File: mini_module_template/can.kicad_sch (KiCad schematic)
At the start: 8 parts, among them SW4 SW_DIP_x01, U4 SN65HVD232

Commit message: Leyout rev 1
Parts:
- removed C14: 100n, Capacitor_SMD:C_0402_1005Metric, symbol Device:C
- removed U4: SN65HVD232, Package_SO:SOIC-8_3.9x4.9mm_P1.27mm, symbol Interface_CAN_LIN:SN65HVD232
- added C36: 100n, Capacitor_SMD:C_0402_1005Metric, symbol Device:C
- added IC1: TJA1044GTK_3Z, SON65P300X300X100-9N-D, symbol TJA1044GTK_3Z:TJA1044GTK_3Z
- added R38: 10k, Resistor_SMD:R_0402_1005Metric, symbol Device:R
- renumbered D3 to D8, D4 to D9, R9 to R36, R20 to R37, R21 to R39
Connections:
- net +3V3: now also IC1.5 (VIO)
- net CAN_H: now also SW4.2, IC1.7 (CANH); no longer R39.1
- net CAN_L: now also R39.1, IC1.6 (CANL); no longer SW4.2
- net CAN_RXD: now also IC1.4 (RXD)
- net CAN_TXD: now also IC1.1 (TXD)
- net GND: now also C36.2, IC1.2 (GND), R38.1
- new net: IC1.8 (STB), R38.2
- new net +5V: C36.1, IC1.3 (VCC)
- no-connect marks 0 -> 1
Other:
- moved on the sheet: R39, SW4

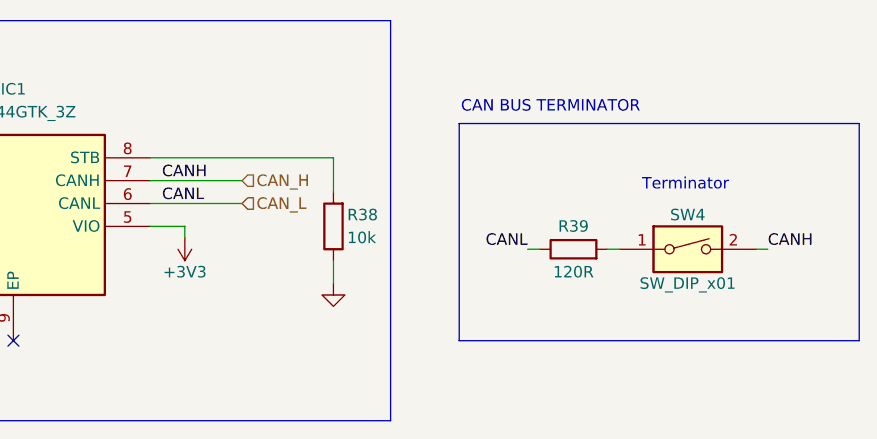
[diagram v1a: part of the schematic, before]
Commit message: fixed can and usb traces
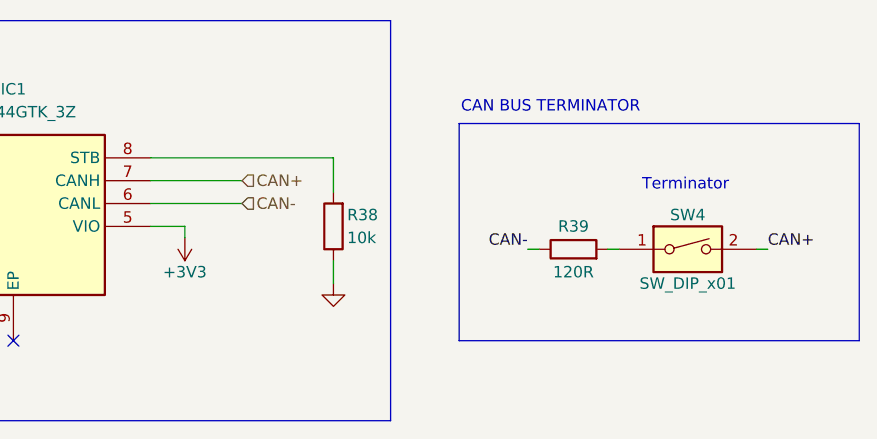
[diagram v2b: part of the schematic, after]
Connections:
- net CAN_H renamed CAN+
- net CAN_L renamed CAN-
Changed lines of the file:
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@@
 		)
 	)
-	(label "CANL"
-		(at 187.96 87.63 0)
-		(fields_autoplaced yes)
-		(effects
-			(font
-				(size 1.27 1.27)
-			)
-			(justify left bottom)
-		)
-	)
-	(label "CANL"
+	(label "CAN-"
 		(at 228.6 92.71 180)
 		(fields_autoplaced yes)
@@
 		)
 	)
-	(label "CANH"
-		(at 187.96 85.09 0)
-		(fields_autoplaced yes)
-		(effects
-			(font
-				(size 1.27 1.27)
-			)
-			(justify left bottom)
-		)
-	)
-	(label "CANH"
+	(label "CAN+"
 		(at 255.27 92.71 0)
 		(fields_autoplaced yes)
@@
 		)
 	)
-	(hierarchical_label "CAN_L"
+	(hierarchical_label "CAN-"
 		(shape input)
 		(at 196.85 87.63 0)
@@
 		)
 	)
-	(hierarchical_label "CAN_H"
+	(hierarchical_label "CAN+"
 		(shape input)
 		(at 196.85 85.09 0)

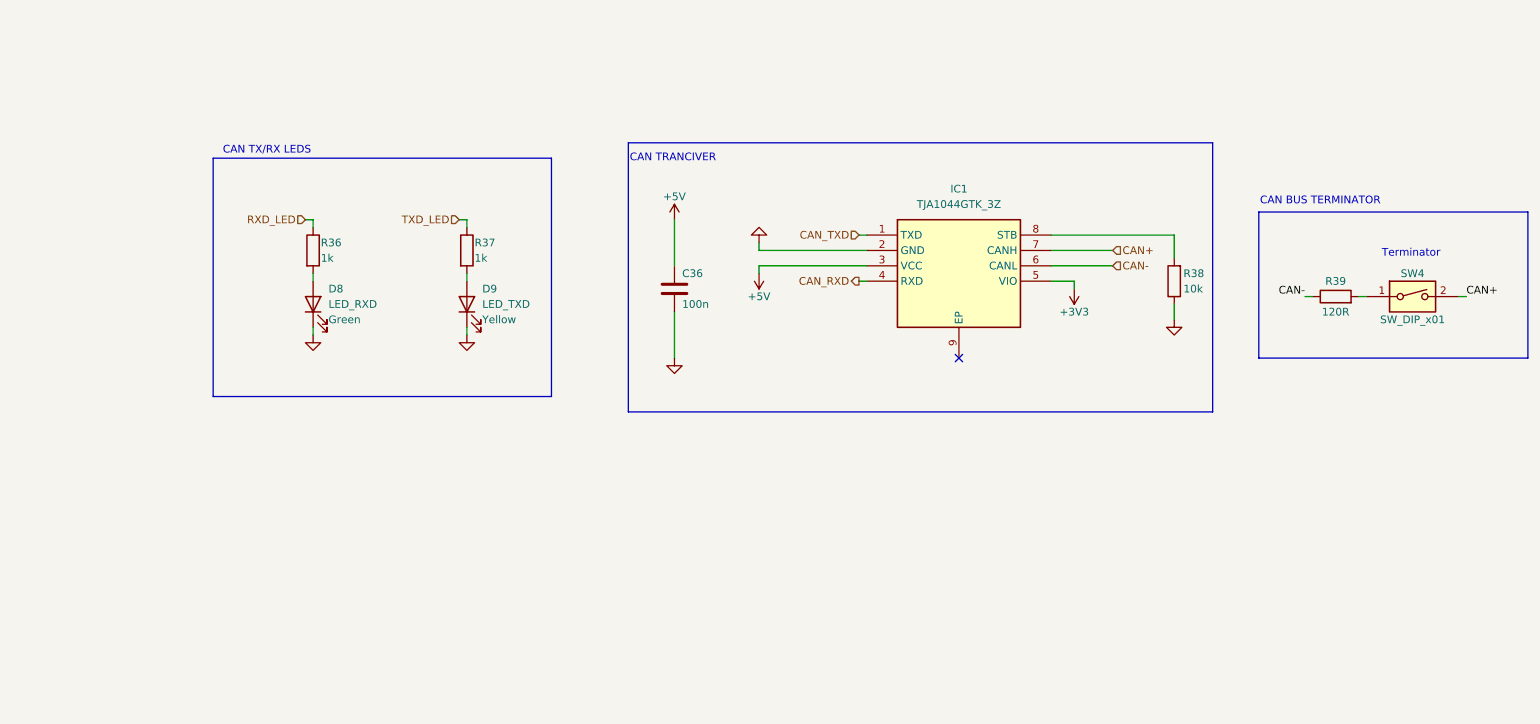
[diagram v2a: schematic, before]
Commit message: revison C, aded 2 can support and gight voltage input stepdown
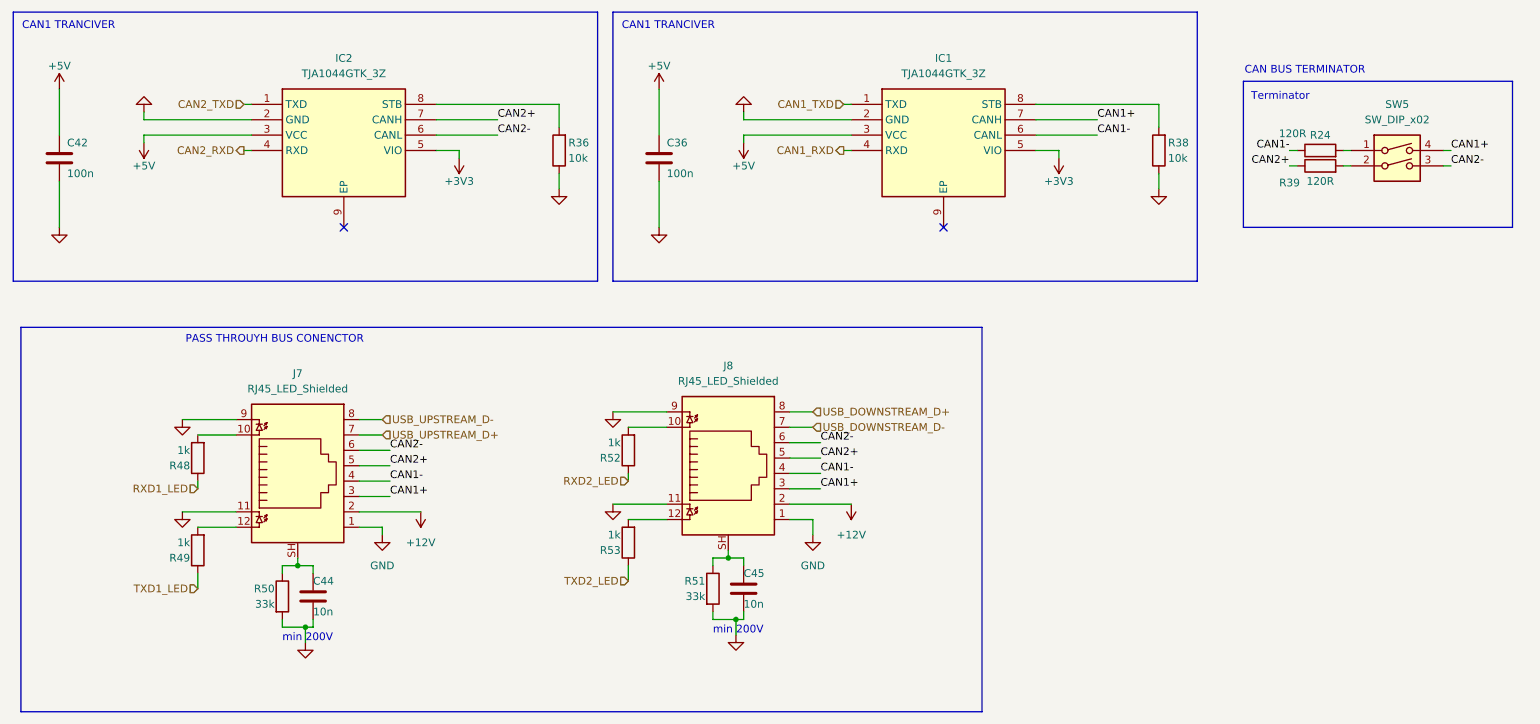
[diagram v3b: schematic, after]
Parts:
- removed D8: LED_RXD, Diode_SMD:D_0603_1608Metric, symbol Device:LED
- removed D9: LED_TXD, Diode_SMD:D_0603_1608Metric, symbol Device:LED
- removed R37: 1k, Resistor_SMD:R_0402_1005Metric, symbol Device:R
- removed SW4: SW_DIP_x01, Button_Switch_SMD:SW_DIP_SPSTx01_Slide_6.7x4.1mm_W6.73mm_P2.54mm_LowProfile_JPin, symbol Switch:SW_DIP_x01
- added C42: 100n, Capacitor_SMD:C_0402_1005Metric, symbol Device:C
- added C44, C45: 10n, Capacitor_SMD:C_0402_1005Metric, symbol Device:C
- added IC2: TJA1044GTK_3Z, SON65P300X300X100-9N-D, symbol TJA1044GTK_3Z:TJA1044GTK_3Z
- added J7, J8: RJ45_LED_Shielded, Connector_RJ:RJ45_Amphenol_RJHSE538X, symbol Connector:RJ45_LED_Shielded
- added R24: 120R, Resistor_SMD:R_0603_1608Metric, symbol Device:R
- added R48, R49, R52, R53: 1k, Resistor_SMD:R_0402_1005Metric, symbol Device:R
- added R50, R51: 33k, Resistor_SMD:R_0402_1005Metric, symbol Device:R
- added SW5: SW_DIP_x02, Button_Switch_THT:SW_DIP_SPSTx02_Slide_6.7x6.64mm_W7.62mm_P2.54mm_LowProfile, symbol Switch:SW_DIP_x02
- R36: value 1k -> 10k
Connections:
- net RXD_LED is gone; now on net GND: R36.1
- net +3V3: now also IC2.5 (VIO)
- net +5V: now also C42.1, IC2.3 (VCC)
- net GND: now also C42.2, C44.2, C45.2, IC2.2 (GND), J7.1, J7.11, J7.9, J8.1, J8.11, J8.9, R50.2, R51.2
- net at R39.2: now also SW5.2
- net at R36.2: now also IC2.8 (STB)
- net CAN+ renamed CAN1+
- net CAN1+: now also J7.3, J8.3, SW5.4
- net CAN- renamed CAN1-
- net CAN1-: now also J7.4, J8.4, R24.1; no longer R39.1
- net CAN_RXD renamed CAN1_RXD
- net CAN_TXD renamed CAN1_TXD
- new net: J8.10, R52.2
- new net: J8.12, R53.2
- new net: C45.1, J8.SH, R51.1
- new net: J7.10, R48.2
- new net: J7.12, R49.2
- new net: C44.1, J7.SH, R50.1
- new net: R24.2, SW5.1
- new net +12V: J7.2, J8.2
- new net CAN2+: IC2.7 (CANH), J7.5, J8.5, R39.1
- new net CAN2-: IC2.6 (CANL), J7.6, J8.6, SW5.3
- new net CAN2_RXD: IC2.4 (RXD)
- new net CAN2_TXD: IC2.1 (TXD)
- new net RXD1_LED: R48.1
- new net RXD2_LED: R52.1
- new net TXD1_LED: R49.1
- new net TXD2_LED: R53.1
- new net USB_DOWNSTREAM_D+: J8.8
- new net USB_DOWNSTREAM_D-: J8.7
- new net USB_UPSTREAM_D+: J7.7
- new net USB_UPSTREAM_D-: J7.8
- no-connect marks 1 -> 2
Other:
- note added: "CAN1 TRANCIVER"
- note added: "PASS THROUYH BUS CONENCTOR"
- note added: "min 200V"
- note removed: "CAN TRANCIVER"
- note removed: "CAN TX/RX LEDS"
- moved on the sheet: C36, IC1, R38, R39

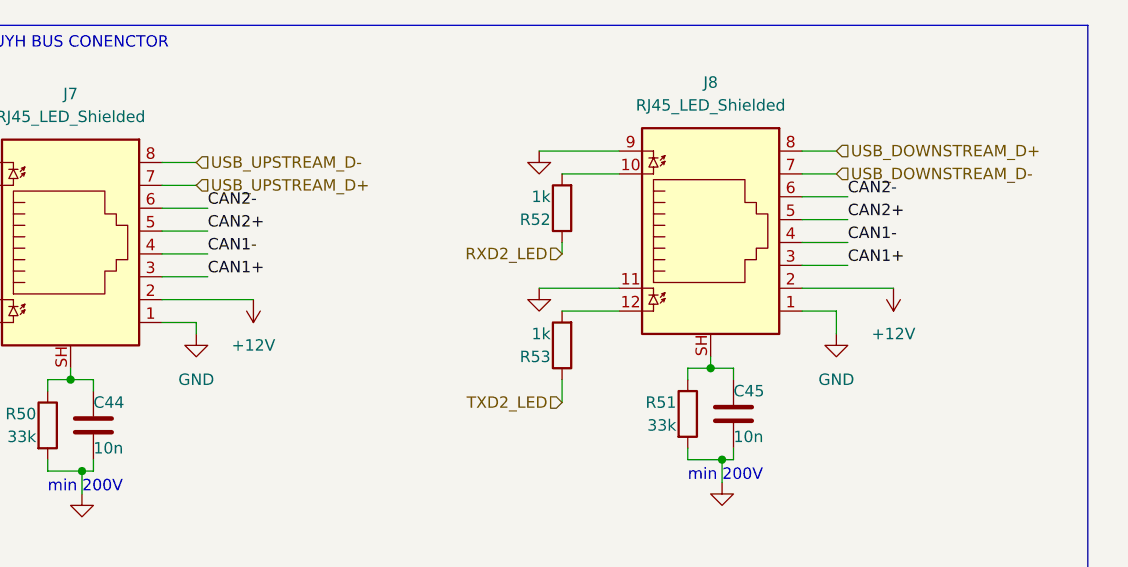
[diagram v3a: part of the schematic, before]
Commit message: changed rj45 conenctor to use differnt pinout with can
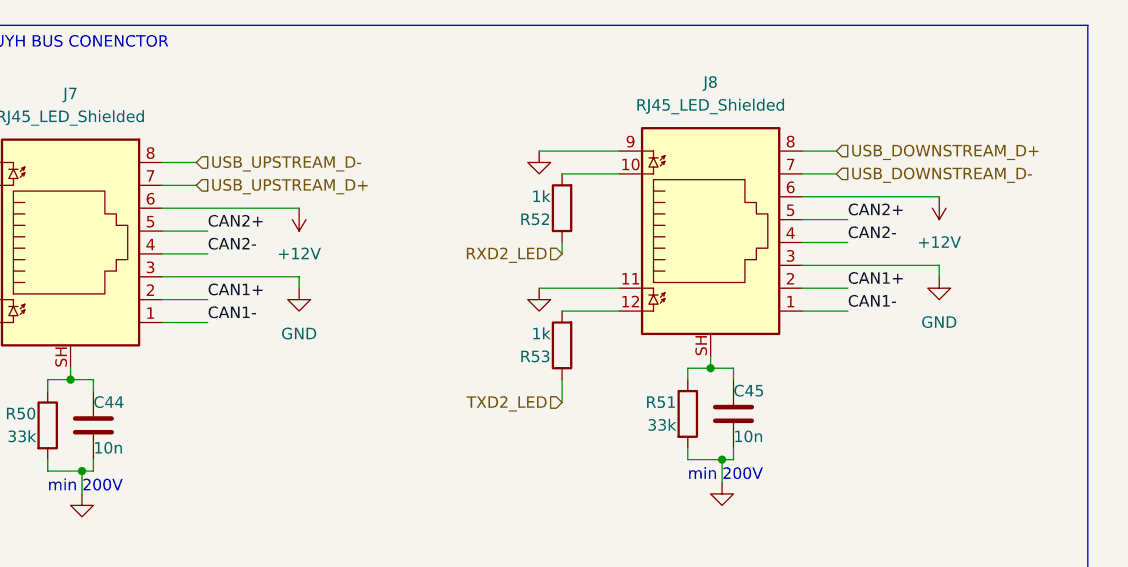
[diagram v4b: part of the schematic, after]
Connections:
- net +12V: now also J7.6, J8.6; no longer J7.2, J8.2
- net CAN1+: now also J7.2, J8.2; no longer J7.3, J8.3
- net CAN1-: now also J7.1, J8.1; no longer J7.4, J8.4
- net CAN2-: now also J7.4, J8.4; no longer J7.6, J8.6
- net GND: now also J7.3, J8.3; no longer J7.1, J8.1

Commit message: fixed issue woth oncvorrect usb pin
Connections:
- net USB_UPSTREAM_D+: now also J7.8; no longer J7.7
- net USB_UPSTREAM_D-: now also J7.7; no longer J7.8
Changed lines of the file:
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@@
 		)
 	)
-	(hierarchical_label "USB_UPSTREAM_D+"
+	(hierarchical_label "USB_UPSTREAM_D-"
 		(shape input)
 		(at 76.2 115.57 0)
@@
 		)
 	)
+	(hierarchical_label "USB_UPSTREAM_D+"
+		(shape input)
+		(at 76.2 113.03 0)
+		(fields_autoplaced yes)
+		(effects
+			(font
+				(size 1.27 1.27)
+			)
+			(justify left)
+		)
+	)
 	(hierarchical_label "CAN2_TXD"
 		(shape input)
@@
 		)
 	)
-	(hierarchical_label "USB_UPSTREAM_D-"
-		(shape input)
-		(at 76.2 113.03 0)
-		(fields_autoplaced yes)
-		(effects
-			(font
-				(size 1.27 1.27)
-			)
-			(justify left)
-		)
-	)

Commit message: updaet schematic
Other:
- company: (none) -> Patryk Dudziński
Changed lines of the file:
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@@
 	(title_block
 		(title "CAN")
+		(date "2025-01-10")
+		(rev "1.0")
+		(company "Patryk Dudziński")
 	)
 	(junction
@@
 	(label "CAN1+"
 		(at 252.73 68.58 0)
-		(fields_autoplaced yes)
 		(effects
 			(font
@@
 	(label "CAN1-"
 		(at 148.59 129.54 0)
-		(fields_autoplaced yes)
 		(effects
 			(font
@@
 	(label "CAN2-"
 		(at 95.25 66.04 0)
-		(fields_autoplaced yes)
 		(effects
 			(font
@@
 	(label "CAN2+"
 		(at 226.06 71.12 180)
-		(fields_autoplaced yes)
 		(effects
 			(font
@@
 	(label "CAN1-"
 		(at 226.06 68.58 180)
-		(fields_autoplaced yes)
 		(effects
 			(font
@@
 	(label "CAN2+"
 		(at 95.25 63.5 0)
-		(fields_autoplaced yes)
 		(effects
 			(font
@@
 	(label "CAN2+"
 		(at 77.47 120.65 0)
-		(fields_autoplaced yes)
 		(effects
 			(font
@@
 	(label "CAN2-"
 		(at 148.59 121.92 0)
-		(fields_autoplaced yes)
 		(effects
 			(font
@@
 	(label "CAN1-"
 		(at 77.47 130.81 0)
-		(fields_autoplaced yes)
 		(effects
 			(font
@@
 	(label "CAN1-"
 		(at 194.31 66.04 0)
-		(fields_autoplaced yes)
 		(effects
 			(font
@@
 	(label "CAN1+"
 		(at 194.31 63.5 0)
-		(fields_autoplaced yes)
 		(effects
 			(font
@@
 	(label "CAN2-"
 		(at 252.73 71.12 0)
-		(fields_autoplaced yes)
 		(effects
 			(font
@@
 	(label "CAN1+"
 		(at 148.59 127 0)
-		(fields_autoplaced yes)
 		(effects
 			(font
@@
 	(label "CAN1+"
 		(at 77.47 128.27 0)
-		(fields_autoplaced yes)
 		(effects
 			(font
@@
 	(label "CAN2-"
 		(at 77.47 123.19 0)
-		(fields_autoplaced yes)
 		(effects
 			(font
@@
 	(label "CAN2+"
 		(at 148.59 119.38 0)
-		(fields_autoplaced yes)
 		(effects
 			(font
@@
 		(shape input)
 		(at 116.84 139.7 180)
-		(fields_autoplaced yes)
 		(effects
 			(font
@@
 		(shape output)
 		(at 53.34 68.58 180)
-		(fields_autoplaced yes)
 		(effects
 			(font
@@
 		(shape input)
 		(at 147.32 114.3 0)
-		(fields_autoplaced yes)
 		(effects
 			(font
@@
 		(shape input)
 		(at 76.2 115.57 0)
-		(fields_autoplaced yes)
 		(effects
 			(font
@@
 		(shape input)
 		(at 116.84 123.19 180)
-		(fields_autoplaced yes)
 		(effects
 			(font
@@
 		(shape input)
 		(at 147.32 111.76 0)
-		(fields_autoplaced yes)
 		(effects
 			(font
@@
 		(shape input)
 		(at 45.72 140.97 180)
-		(fields_autoplaced yes)
 		(effects
 			(font
@@
 		(shape input)
 		(at 76.2 113.03 0)
-		(fields_autoplaced yes)
 		(effects
 			(font
@@
 		(shape input)
 		(at 53.34 60.96 180)
-		(fields_autoplaced yes)
 		(effects
 			(font
@@
 		(shape output)
 		(at 152.4 68.58 180)
-		(fields_autoplaced yes)
 		(effects
 			(font
@@
 		(shape input)
 		(at 152.4 60.96 180)
-		(fields_autoplaced yes)
 		(effects
 			(font
@@
 		(shape input)
 		(at 45.72 124.46 180)
-		(fields_autoplaced yes)
-		(effects
-			(font
+		(effects
+			(font
